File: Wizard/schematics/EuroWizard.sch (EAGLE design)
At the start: 127 parts, among them IC1 MC7805CDTG, IC2 NE5532D, IC3 NE5532D, IC4 QUAD_OPAMPD, IC5 LM4040B10, Q1 BSS123, Q2 SI2309CDS, Q3 BC846, Q903 BC846, SW1 B3F-1000, SW2 B3F-1000, SW3 B3F-1000, SW4 B3F-1000, SW5 B3F-1000, U3 MIC2005, X3 KUSBVX, X5 USBPTH-VERTICAL

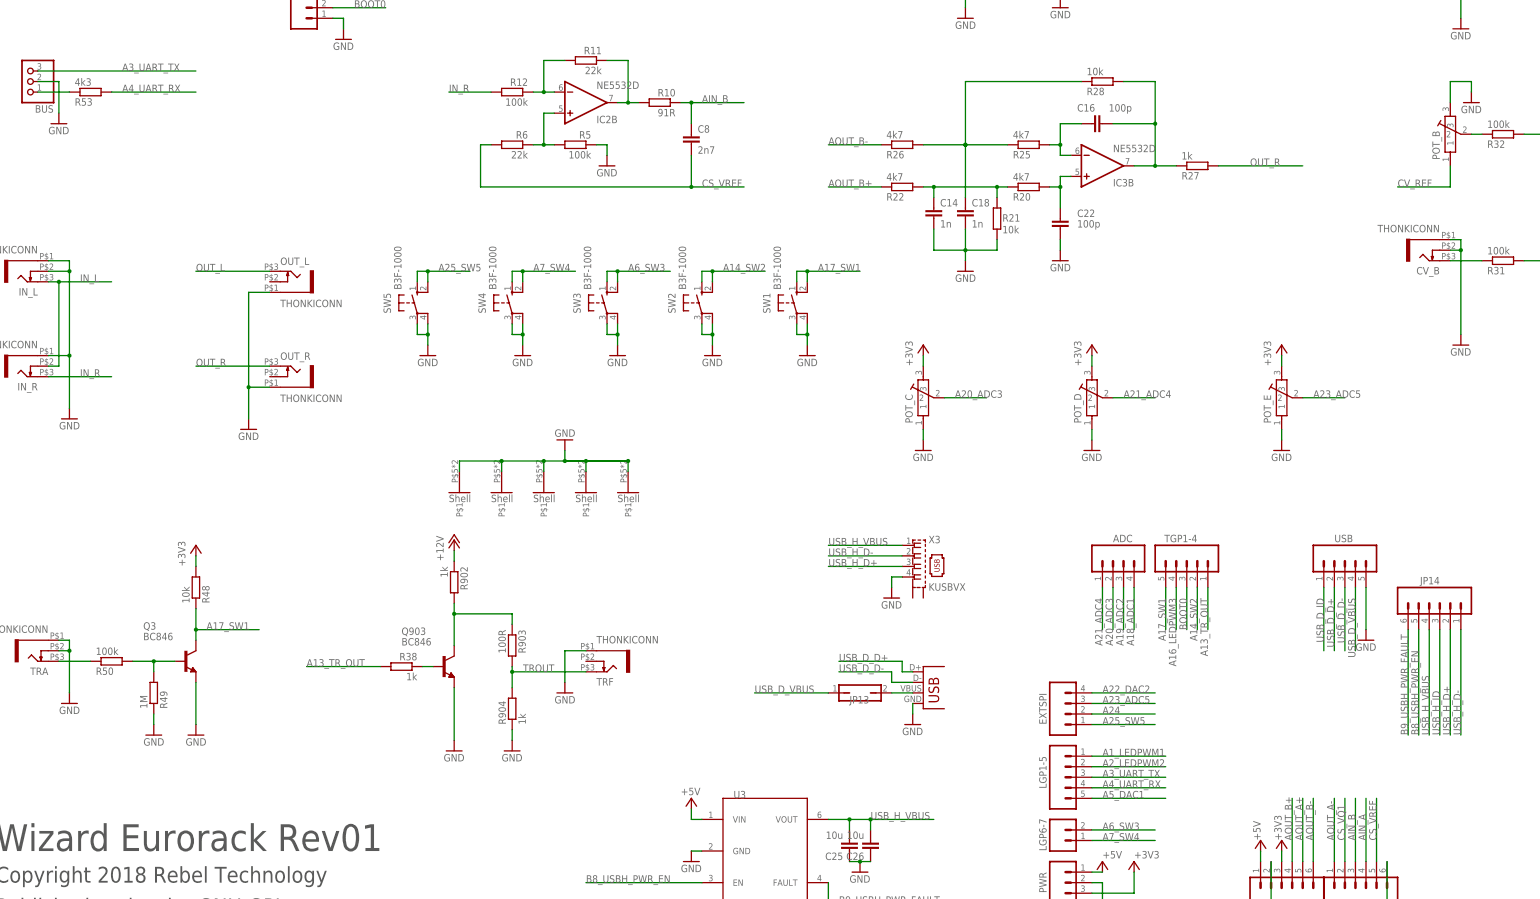
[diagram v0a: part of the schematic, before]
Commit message: updated USB names and fixed a resistor value
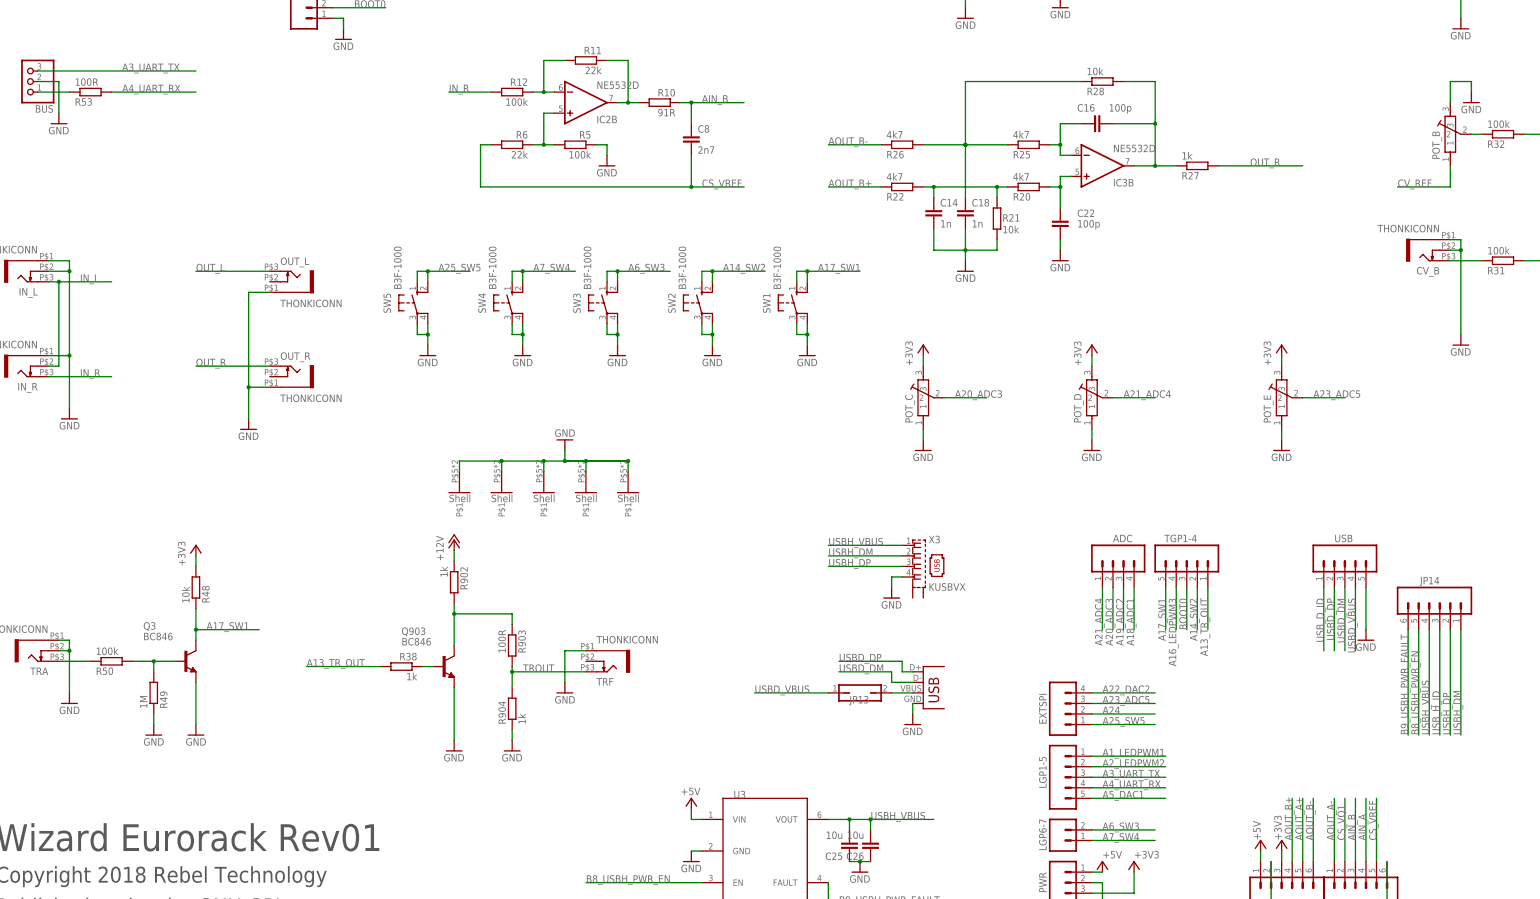
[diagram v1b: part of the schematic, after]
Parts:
- R53: value 4k3 -> 100R
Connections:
- net USB_D_D+ renamed USBD_DP
- net USB_D_D- renamed USBD_DM
- net USB_D_VBUS renamed USBD_VBUS
- net USB_H_D+ renamed USBH_DP
- net USB_H_D- renamed USBH_DM
- net USB_H_VBUS renamed USBH_VBUS
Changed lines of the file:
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@@
 <part name="GND84" library="supply1" deviceset="GND" device=""/>
 <part name="BUS" library="Rebel" deviceset="CON-JST-1X03" device="PH-TH"/>
-<part name="R53" library="Rebel" deviceset="R-EU_" device="0603" value="4k3"/>
+<part name="R53" library="Rebel" deviceset="R-EU_" device="0603" value="100R"/>
 <part name="POT_E" library="Rebel" deviceset="POT-ALPS-RK09L" device="1140"/>
 <part name="+3V1" library="supply1" deviceset="+3V3" device=""/>
@@
 </segment>
 </net>
-<net name="USB_D_D+" class="0">
+<net name="USBD_DP" class="0">
 <segment>
 <pinref part="USB" gate="G$1" pin="2"/>
@@
 </segment>
 </net>
-<net name="USB_D_VBUS" class="0">
+<net name="USBD_VBUS" class="0">
 <segment>
 <pinref part="USB" gate="G$1" pin="4"/>
@@
 </segment>
 </net>
-<net name="USB_D_D-" class="0">
+<net name="USBD_DM" class="0">
 <segment>
 <pinref part="USB" gate="G$1" pin="3"/>
@@
 </segment>
 </net>
-<net name="USB_H_D-" class="0">
+<net name="USBH_DM" class="0">
 <segment>
 <label x="287.02" y="5.08" size="1.778" layer="95" rot="R90"/>
@@
 </segment>
 </net>
-<net name="USB_H_D+" class="0">
+<net name="USBH_DP" class="0">
 <segment>
 <label x="284.48" y="5.08" size="1.778" layer="95" rot="R90"/>
@@
 </segment>
 </net>
-<net name="USB_H_VBUS" class="0">
+<net name="USBH_VBUS" class="0">
 <segment>
 <label x="279.4" y="5.08" size="1.778" layer="95" rot="R90"/>

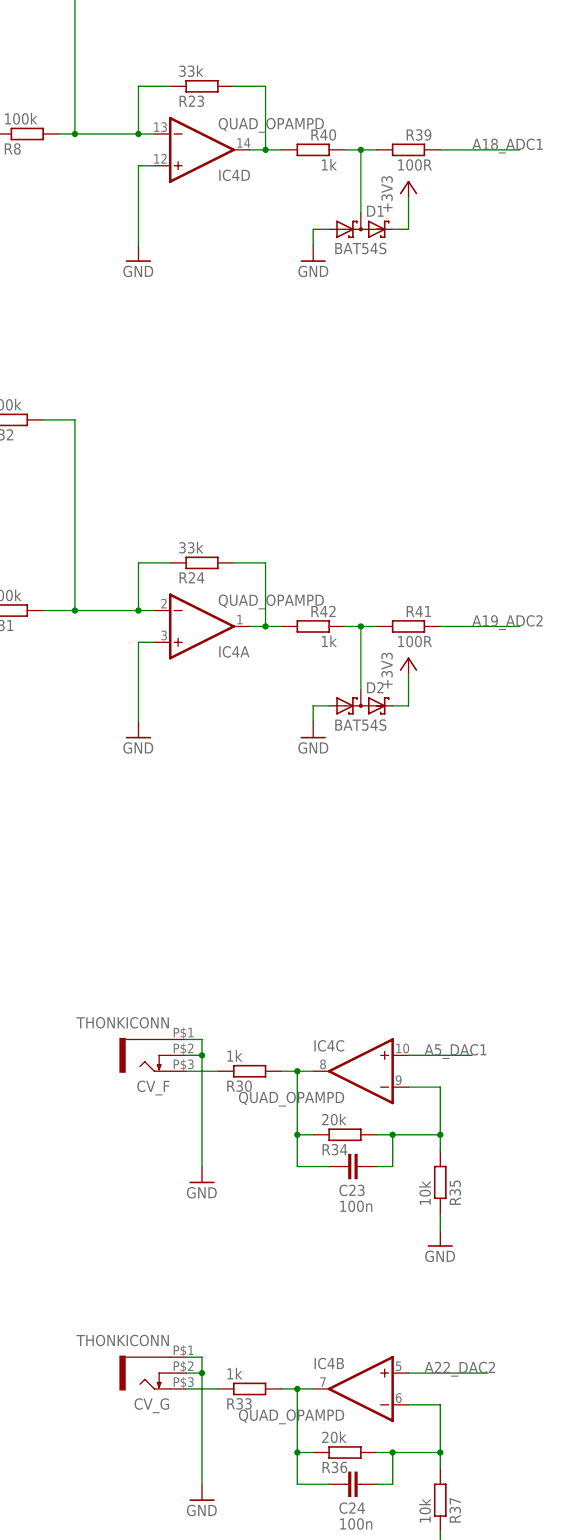
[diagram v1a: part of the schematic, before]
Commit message: specified op amps as TL074
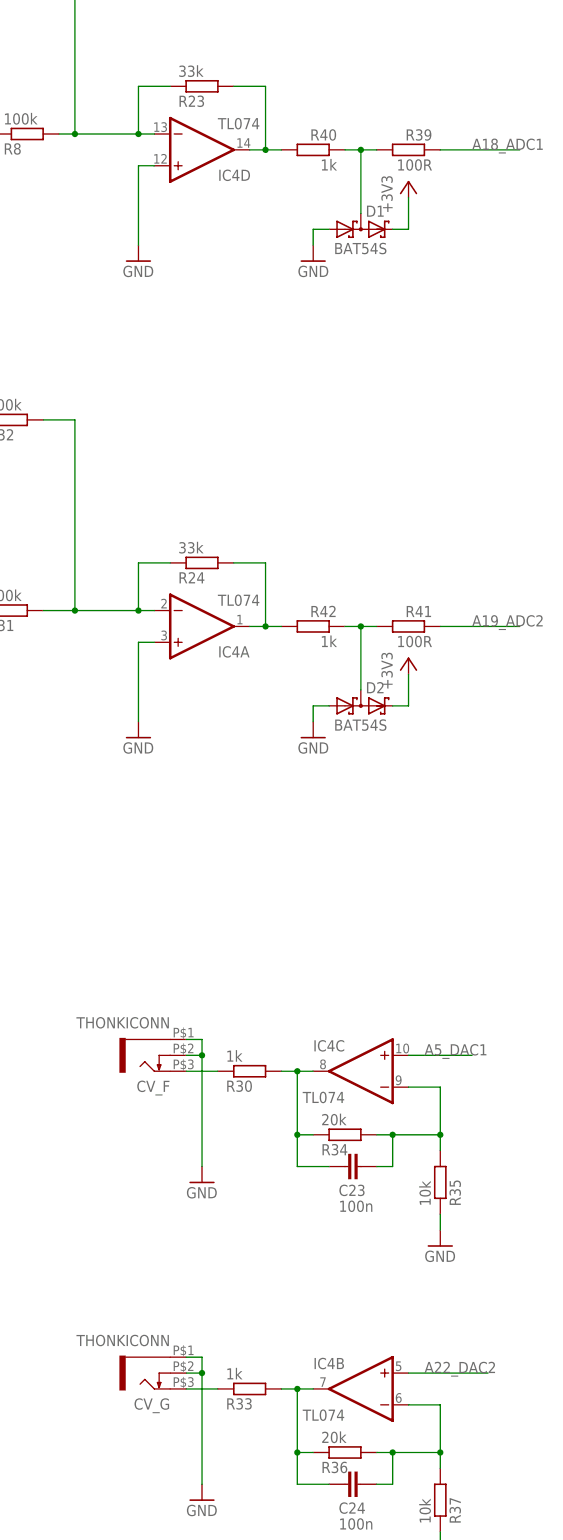
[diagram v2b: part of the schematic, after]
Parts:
- IC4: value QUAD_OPAMPD -> TL074
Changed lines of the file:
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@@
 <?xml version="1.0" encoding="utf-8"?>
 <!DOCTYPE eagle SYSTEM "eagle.dtd">
-<eagle version="9.2.1">
+<eagle version="9.5.2">
 <drawing>
 <settings>
@@
 <part name="GND19" library="supply1" deviceset="GND" device=""/>
 <part name="GND14" library="supply1" deviceset="GND" device=""/>
-<part name="IC4" library="adafruit" deviceset="QUAD_OPAMP" device="D" value="QUAD_OPAMPD"/>
+<part name="IC4" library="adafruit" deviceset="QUAD_OPAMP" device="D" value="TL074"/>
 <part name="R8" library="Rebel" deviceset="R-EU_" device="0603" value="100k"/>
 <part name="R9" library="Rebel" deviceset="R-EU_" device="0603" value="100k"/>

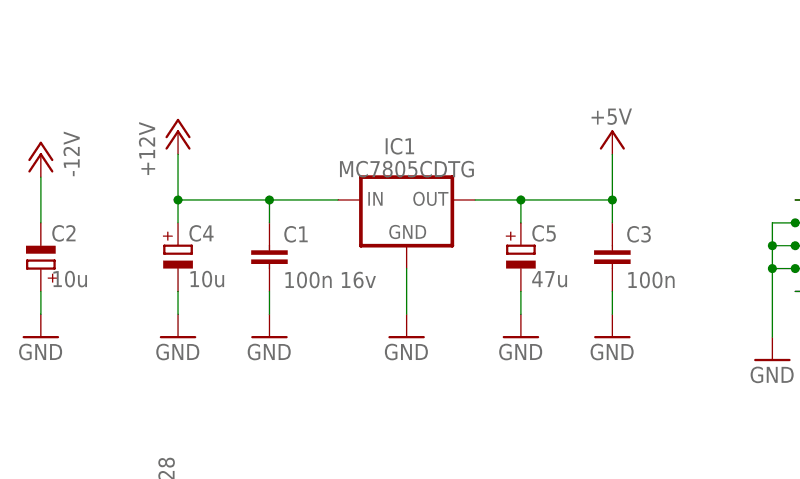
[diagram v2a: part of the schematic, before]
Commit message: rotated power inlet, changed to TO220 regulator, changed some routing
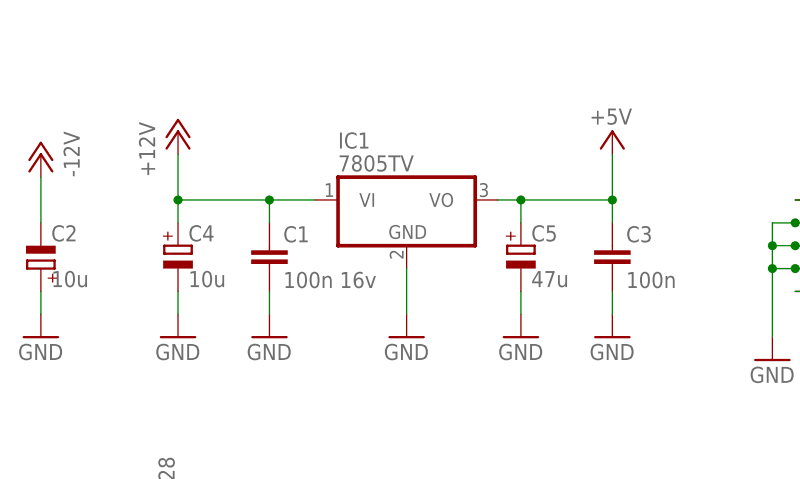
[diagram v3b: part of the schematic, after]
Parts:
- C2, C4: device Rebel:CPOL-EU153CLV-0505 -> Rebel:CPOL-EUUD-4X5,8
- C5: device rcl:CPOL-EUB -> rcl:CPOL-EUUD-4X5,8
- IC1: value MC7805CDTG -> 7805TV; device James:MC78XX -> linear:7805TV; OC_FARNELL 2296028 -> (none)
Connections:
- net +12V: now also IC1.VI; no longer IC1.IN
- net +5V: now also IC1.VO; no longer IC1.OUT
